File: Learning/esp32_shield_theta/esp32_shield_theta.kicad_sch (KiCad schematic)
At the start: 16 parts, among them J1 Conn_01x06, J2 DE9_Plug, U1 ESP32-DEVKIT-V1, U2 LM358

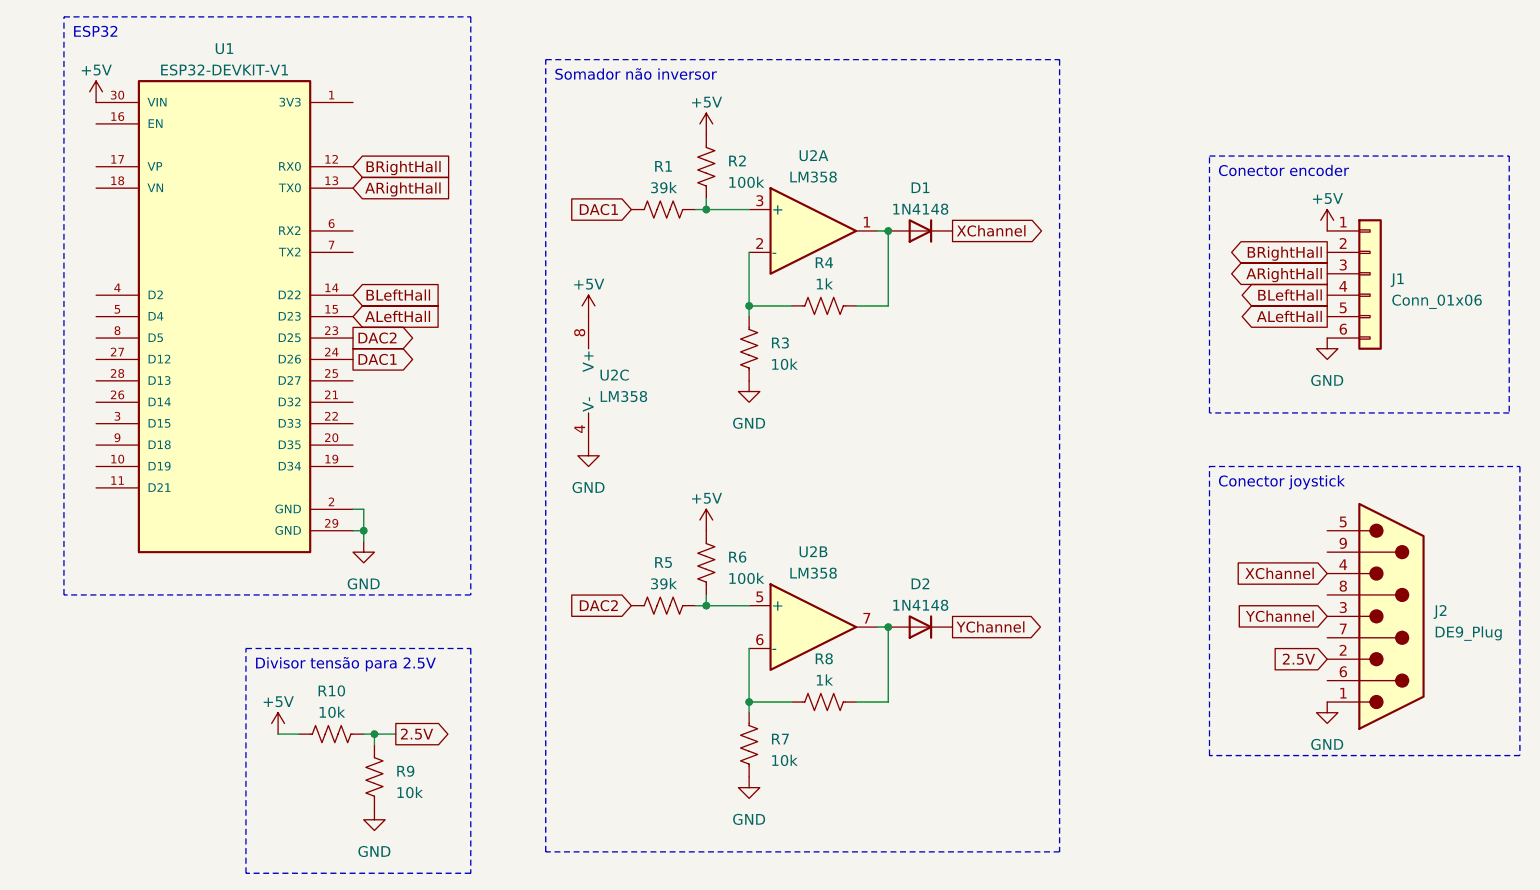
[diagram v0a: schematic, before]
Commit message: Update on esp32 theta
change to a up to date version
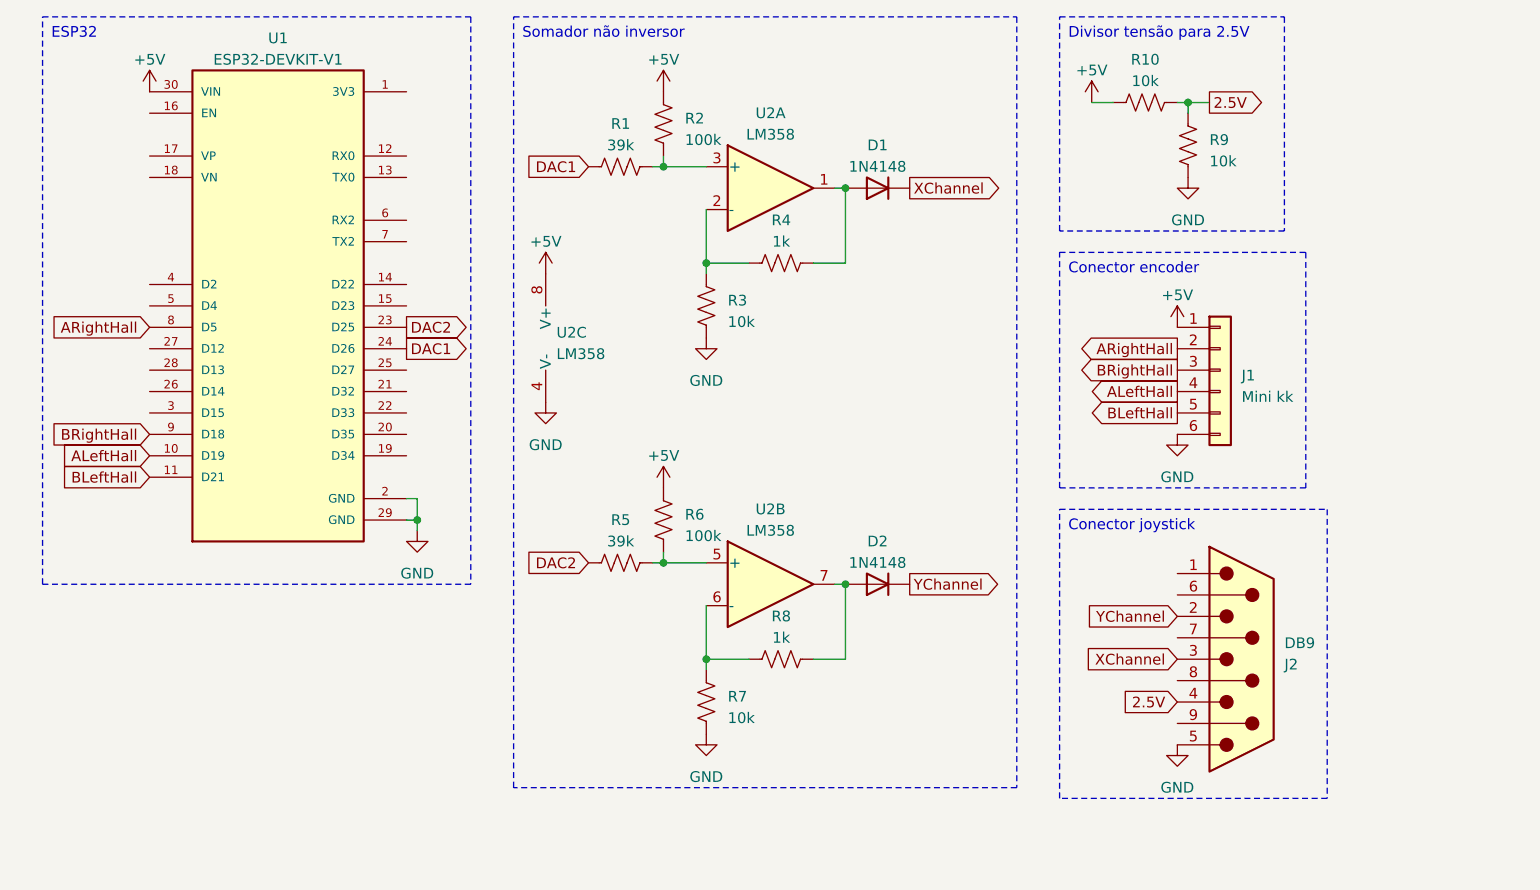
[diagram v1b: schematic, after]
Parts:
- J1: value Conn_01x06 -> Mini kk
- J2: value DE9_Plug -> DB9
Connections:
- net 2.5V: now also J2.4; no longer J2.2
- net ALeftHall: now also J1.4 (Pin_4), U1.10 (D19); no longer J1.5 (Pin_5), U1.15 (D23)
- net ARightHall: now also J1.2 (Pin_2), U1.8 (D5); no longer J1.3 (Pin_3), U1.13 (TX0)
- net BLeftHall: now also J1.5 (Pin_5), U1.11 (D21); no longer J1.4 (Pin_4), U1.14 (D22)
- net BRightHall: now also J1.3 (Pin_3), U1.9 (D18); no longer J1.2 (Pin_2), U1.12 (RX0)
- net GND: now also J2.5; no longer J2.1
- net XChannel: now also J2.3; no longer J2.4
- net YChannel: now also J2.2; no longer J2.3
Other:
- moved on the sheet: D1, D2, J1, J2, R1, R10, R2, R3, R4, R5, R6, R7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
